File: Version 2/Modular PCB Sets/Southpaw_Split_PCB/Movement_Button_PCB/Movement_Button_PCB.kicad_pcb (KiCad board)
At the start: 2 copper layers, 114 x 98 mm, 13 parts, among them J1 Conn_01x06_Socket

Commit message: general part layout
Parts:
- moved J1 29.0 mm to (107.0, 99.0)
- moved R14 10.2 mm to (133.9, 80.0), turned to 0 degrees
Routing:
- net /Gnd: track 158.5 -> 0.00 mm
- net /3v3: track 133.0 -> 0.00 mm, vias 1 -> 0
- net /Right: track 97.2 -> 0.00 mm
- net /Up: track 74.0 -> 0.00 mm
- net /Down: track 58.7 -> 0.00 mm
- net /Left: track 36.4 -> 0.00 mm
- net Net-(D9-A): track 15.9 -> 0.00 mm
- net Net-(D13-A): track 5.33 -> 0.00 mm
- net Net-(D12-A): track 5.25 -> 0.00 mm
- net Net-(D11-A): track 5.25 -> 0.00 mm

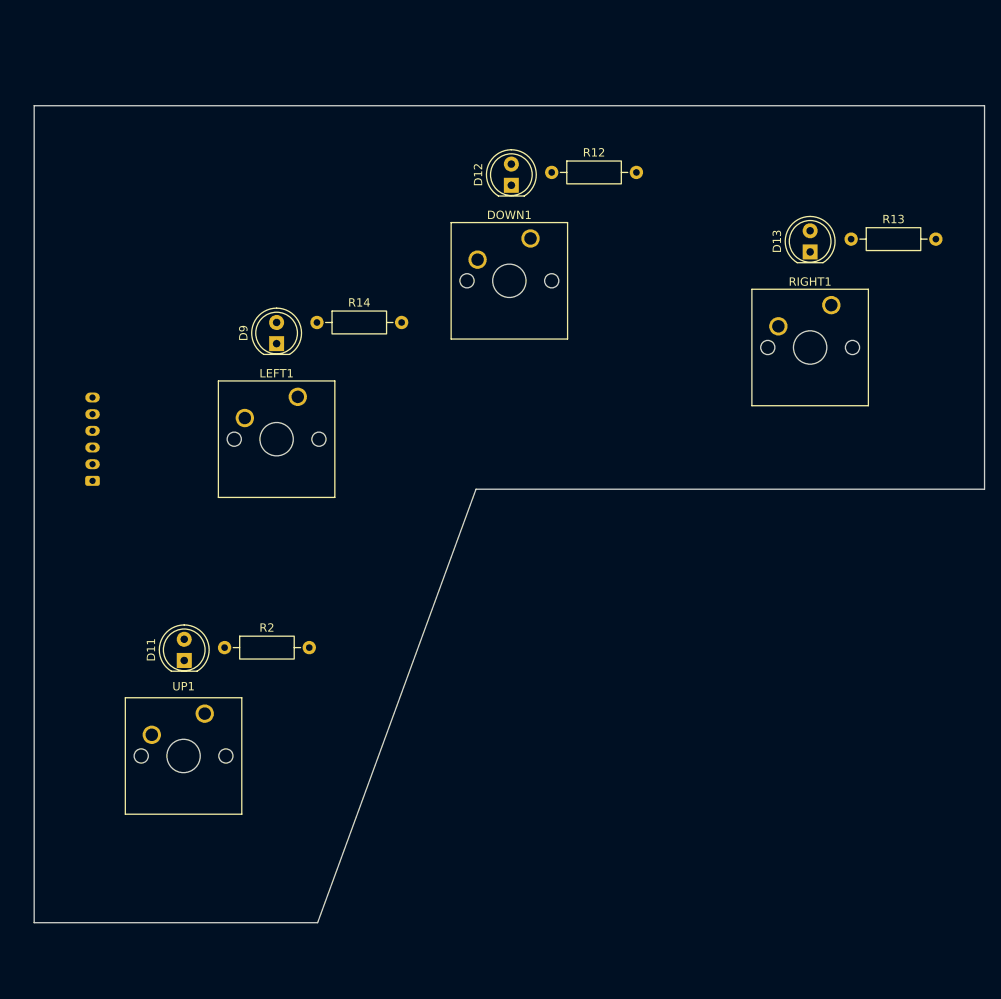
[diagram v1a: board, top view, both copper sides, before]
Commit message: finished movement pcb, need to make some small adjustments to action pcb
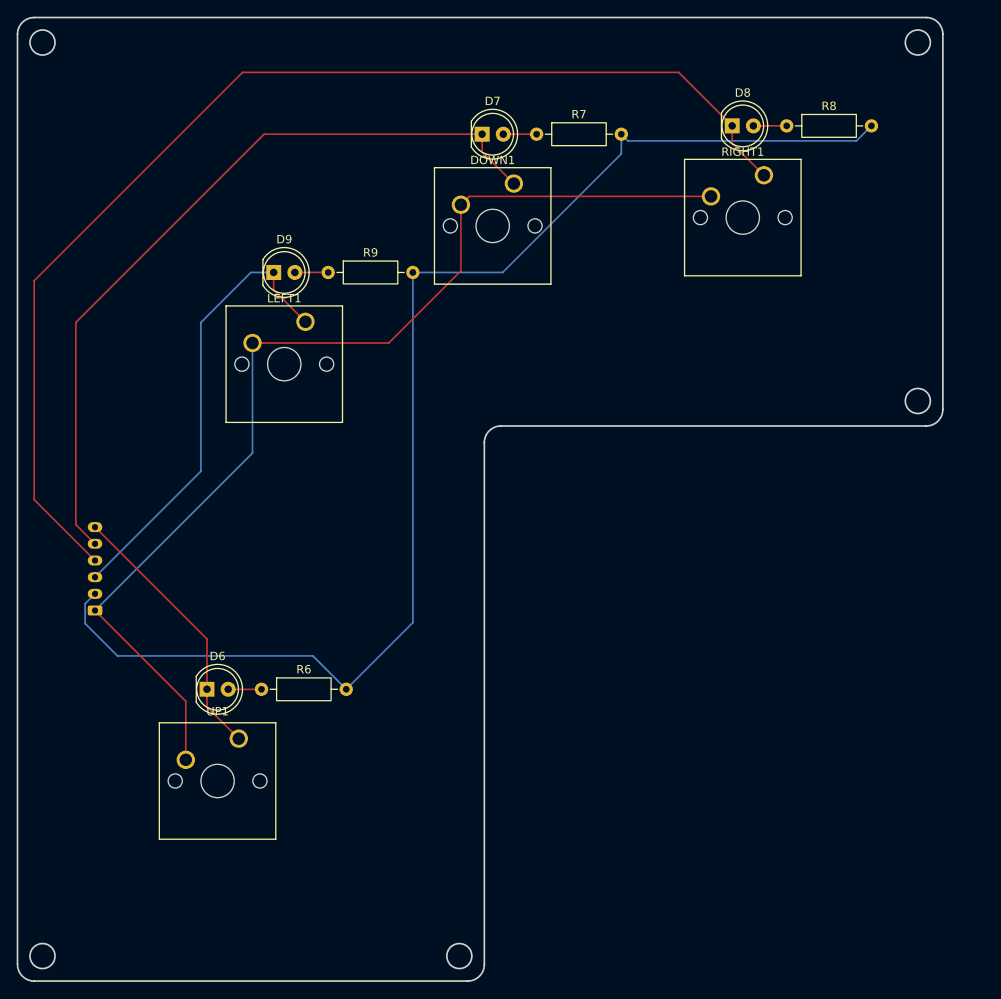
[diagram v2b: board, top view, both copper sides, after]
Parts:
- moved D8 17.8 mm to (183.7, 56.4), turned to 0 degrees
- moved RIGHT1 17.6 mm to (187.5, 62.3)
- moved R8 15.6 mm to (190.3, 56.4)
- moved J6 15.6 mm to (107.3, 114.5)
- moved LEFT1 9.05 mm to (132.5, 79.9)
- moved D9 8.55 mm to (128.7, 74.0), turned to 0 degrees
- moved D7 7.06 mm to (153.7, 57.4), turned to 0 degrees
- moved DOWN1 6.88 mm to (157.5, 63.3)
- moved R6 6.68 mm to (127.3, 124.0)
- moved R9 6.15 mm to (135.3, 74.0)
- moved UP1 5.06 mm to (124.5, 129.9)
- moved R7 4.93 mm to (160.3, 57.4)
- moved D6 4.41 mm to (120.7, 124.0), turned to 0 degrees
- renumbered D11 to D6, D12 to D7, D13 to D8, J1 to J6, R2 to R6, R12 to R7, R13 to R8, R14 to R9
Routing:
- net /3v3: track 0.00 -> 156.3 mm
- net /Right: track 0.00 -> 140.8 mm
- net /Gnd: track 0.00 -> 129.3 mm
- net /Down: track 0.00 -> 93.1 mm
- net /Left: track 0.00 -> 54.5 mm
- net /Up: track 0.00 -> 32.5 mm
- net Net-(D9-A): track 0.00 -> 4.00 mm
- net Net-(D8-A): track 0.00 -> 4.00 mm
- net Net-(D7-A): track 0.00 -> 4.00 mm
- net Net-(D6-A): track 0.00 -> 4.00 mm
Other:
- board size 114 x 98 mm -> 111 x 115.6 mm

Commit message: Finalized design and uploaded gerbers to JLCpcb, waiting for boards to come in
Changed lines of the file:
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@@
 			(plot_on_all_layers_selection 0x00000000_00000000_00000000_00000000)
 			(disableapertmacros no)
-			(usegerberextensions no)
+			(usegerberextensions yes)
 			(usegerberattributes yes)
 			(usegerberadvancedattributes yes)
-			(creategerberjobfile yes)
+			(creategerberjobfile no)
 			(dashed_line_dash_ratio 12.000000)
 			(dashed_line_gap_ratio 3.000000)
@@
 			(outputformat 1)
 			(mirror no)
-			(drillshape 1)
+			(drillshape 0)
 			(scaleselection 1)
-			(outputdirectory "")
+			(outputdirectory "../Gerbers/Movement_Button_Gerbers/")
 		)
 	)
@@
 		(tags "Cherry MX keyswitch 1.00u PCB")
 		(property "Reference" "DOWN1"
-			(at -2.54 -2.794 0)
+			(at -5.89 -0.27 0)
 			(layer "F.SilkS")
 			(effects
@@
 		)
 		(fp_text user "${REFERENCE}"
-			(at -2.54 -2.794 0)
+			(at -5.89 -0.27 0)
 			(layer "F.Fab")
 			(effects
@@
 		(tags "Cherry MX keyswitch 1.00u PCB")
 		(property "Reference" "LEFT1"
-			(at -2.54 -2.794 0)
+			(at -6.54 -0.27 0)
 			(layer "F.SilkS")
 			(effects
@@
 		)
 		(fp_text user "${REFERENCE}"
-			(at -2.54 -2.794 0)
+			(at -6.54 -0.27 0)
 			(layer "F.Fab")
 			(effects
@@
 		(tags "Cherry MX keyswitch 1.00u PCB")
 		(property "Reference" "UP1"
-			(at -2.54 -3.254 0)
+			(at -6.89 -0.27 0)
 			(layer "F.SilkS")
 			(effects
@@
 		)
 		(fp_text user "${REFERENCE}"
-			(at -2.54 -3.254 0)
+			(at -6.89 -0.27 0)
 			(layer "F.Fab")
 			(effects
@@
 		(tags "Cherry MX keyswitch 1.00u PCB")
 		(property "Reference" "RIGHT1"
-			(at -2.54 -2.794 0)
+			(at -5.89 -0.27 0)
 			(layer "F.SilkS")
 			(effects
@@
 		)
 		(fp_text user "${REFERENCE}"
-			(at -2.54 -2.794 0)
-			(layer "F.Fab")
-			(effects
+			(at -5.89 -0.27 0)
+			(layer "F.Fab")
+			(effects
